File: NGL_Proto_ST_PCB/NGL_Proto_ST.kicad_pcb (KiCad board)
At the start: 2 copper layers, 113 x 70 mm, 138 parts, among them J1 Conn_01x08_Male, J2 Conn_01x04_Male, J3 227161-2, J4 Conn_01x06_Male, J5 Conn_01x04_Male, J6 Conn_01x03_Male, M1 ROB-08449, SW3 SW_Push, SW4 SW_Push, T1 RU1C002UNTCL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

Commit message: Début ajout modifs de la review
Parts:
- removed G2: LOGO, Lib_NGL_EURO:NGL_neg
- added TP10: GND, Connector_PinHeader_2.54mm:PinHeader_1x01_P2.54mm_Vertical, B.Cu at (104.5, 106.0)
- added TP13: GND, Connector_PinHeader_2.54mm:PinHeader_1x01_P2.54mm_Vertical, B.Cu at (103.0, 63.0)
- added TP14: GND, Connector_PinHeader_2.54mm:PinHeader_1x01_P2.54mm_Vertical, B.Cu at (210.0, 64.0)
- added TP9: GND, Connector_PinHeader_2.54mm:PinHeader_1x01_P2.54mm_Vertical, B.Cu at (209.5, 112.5)
- R10P1: value 590 -> NC
- R2: value 442R -> 348R
- R2P1: value 1K -> NC
- TP1: value TestPoint -> IN
- TP11: value TestPoint -> OUT_DIFF
- TP12: value TestPoint -> RECT_DIFF
- TP2: value TestPoint -> IN_ADC
- TP3: value TestPoint -> OUT
- TP4: value TestPoint -> IN_ADC_DIFF
- TP5: value TestPoint -> RECT
- TP6: renamed from TPP3; value TestPointPad -> CLK_GEN
- TP7: value TestPoint -> +3.3V
- TP8: value TestPoint -> -3.3V
- TPP2: value TestPointPad -> +BATT
- TPP4: value TestPointPad -> GND
- moved C16 43.8 mm to (121.2, 92.3), turned to 270 degrees
- moved U6 36.5 mm to (126.4, 91.5)
- moved C17 24.5 mm to (131.8, 94.5), turned to 270 degrees
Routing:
- net -3V3: track 234.2 -> 64.5 mm, vias 6 -> 4
- net +3V3: track 434.9 -> 401.4 mm
- net Net-(C16-Pad2): track 13.4 -> 0.00 mm
- net Net-(C16-Pad1): track 11.3 -> 0.00 mm
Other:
- board text removed: "+3.3V"
- board text removed: "-3.3V"
- board text removed: "DIFF"
- board text removed: "SENS"

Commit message: Commit avand 2° dsn
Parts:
- J2: footprint Connector_PinHeader_2.54mm:PinHeader_1x04_P2.54mm_Vertical -> Connector_PinHeader_2.54mm:PinHeader_1x06_P2.54mm_Vertical
- moved TP9 47.2 mm to (165.8, 94.6)
- moved C7 11.8 mm to (126.5, 57.0), turned to 270 degrees
- moved C4 11.3 mm to (115.0, 60.0), turned to 270 degrees
- moved J2 1.74 mm to (207.5, 108.5)
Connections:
- C19 pad 1: /ESP32/EN -> EN
- J2 pad 2: UART_TX -> BOOT
- J2 pad 3: UART_RX -> UART_TX
- J2 pad 4: +3V3 -> UART_RX
- R17 pad 2: /ESP32/EN -> EN
- SW3 pad 2: /ESP32/EN -> EN
- SW4 pad 1: Net-(SW4-Pad1) -> BOOT
- U4 pad 25: Net-(SW4-Pad1) -> BOOT
- U4 pad 3: /ESP32/EN -> EN
- U4 pad 31: CLOCK_GEN -> Net-(U4-Pad31)
- U4 pad 8: Net-(U4-Pad8) -> CLOCK_GEN
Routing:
- net OUT_NTC: track 131.9 -> 0.00 mm
- net CLOCK_GEN: track 120.4 -> 0.00 mm
- net INH: track 118.2 -> 0.00 mm
- net OUT_BAT: track 107.0 -> 0.00 mm, vias 1 -> 0
- net CLK: track 91.2 -> 0.00 mm, vias 1 -> 0
- net CS_R2: track 90.1 -> 0.00 mm, vias 1 -> 0
- net MOSI: track 82.9 -> 0.00 mm
- net CURRENT_3: track 71.6 -> 0.00 mm, vias 1 -> 0
- net OUT_SENS: track 71.6 -> 0.00 mm, vias 1 -> 0
- net DIFF-: track 63.6 -> 0.00 mm, vias 1 -> 0
- net -3V3: track 64.5 -> 120.6 mm
- net DIFF+: track 53.8 -> 0.00 mm
- net CS_R10: track 53.7 -> 0.00 mm, vias 2 -> 0
- net Net-(JP8-Pad1): track 51.2 -> 0.00 mm, vias 1 -> 0
- net R10_OUT: track 43.6 -> 0.00 mm, vias 1 -> 0
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- removed copper zone on B.Cu, net -BATT
- removed copper zone on F.Cu, net -BATT
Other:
- board text added: "BOOT"
- board text added: "EN"
- board text removed: "MISO"

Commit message: avant 3° DSN
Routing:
- added copper zone on F.Cu, net -BATT
- added copper zone on B.Cu, net Net-(D1-Pad2)
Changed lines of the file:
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@@
     (42 Eco1.User user hide)
     (43 Eco2.User user hide)
-    (44 Edge.Cuts user)
+    (44 Edge.Cuts user hide)
     (45 Margin user hide)
     (46 B.CrtYd user)
@@
     (fp_line (start -1.9939 -2.159) (end -3.0988 -2.159) (layer F.Fab) (width 0.1))
     (fp_line (start -1.9939 -1.651) (end -1.9939 -2.159) (layer F.Fab) (width 0.1))
-    (fp_text user * (at -2.7178 -3.606) (layer F.SilkS)
-      (effects (font (size 1 1) (thickness 0.15)))
-    )
     (fp_text user * (at -5.55 -1.6) (layer F.SilkS)
       (effects (font (size 1 1) (thickness 0.15)))
@@
       (effects (font (size 1 1) (thickness 0.15)))
     )
-    (fp_text user * (at -2.7178 -3.606) (layer F.SilkS)
-      (effects (font (size 1 1) (thickness 0.15)))
-    )
     (fp_text user "Copyright 2021 Accelerated Designs. All rights reserved." (at 0 0) (layer Cmts.User) hide
       (effects (font (size 0.127 0.127) (thickness 0.002)))
@@
       )
     )
+  )
+  (zone (net 11) (net_name -BATT) (layer F.Cu) (hatch edge 0.508)
+    (connect_pads (clearance 0.15))
+    (min_thickness 0.15)
+    (fill yes (arc_segments 32) (thermal_gap 0.2) (thermal_bridge_width 0.2))
+    (polygon
+      (pts
+        (xy 212.5 120) (xy 100 119.5) (xy 99.5 50) (xy 213 50)
+      )
+    )
+  )
+  (zone (net 11) (net_name "Net-(D1-Pad2)") (layer B.Cu) (hatch edge 0.508)
+    (connect_pads (clearance 0.15))
+    (min_thickness 0.15)
+    (fill yes (arc_segments 32) (thermal_gap 0.2) (thermal_bridge_width 0.2))
+    (polygon
+      (pts
+        (xy 212.5 120) (xy 100 119.5) (xy 99.5 50) (xy 213 50)
+      )
+    )

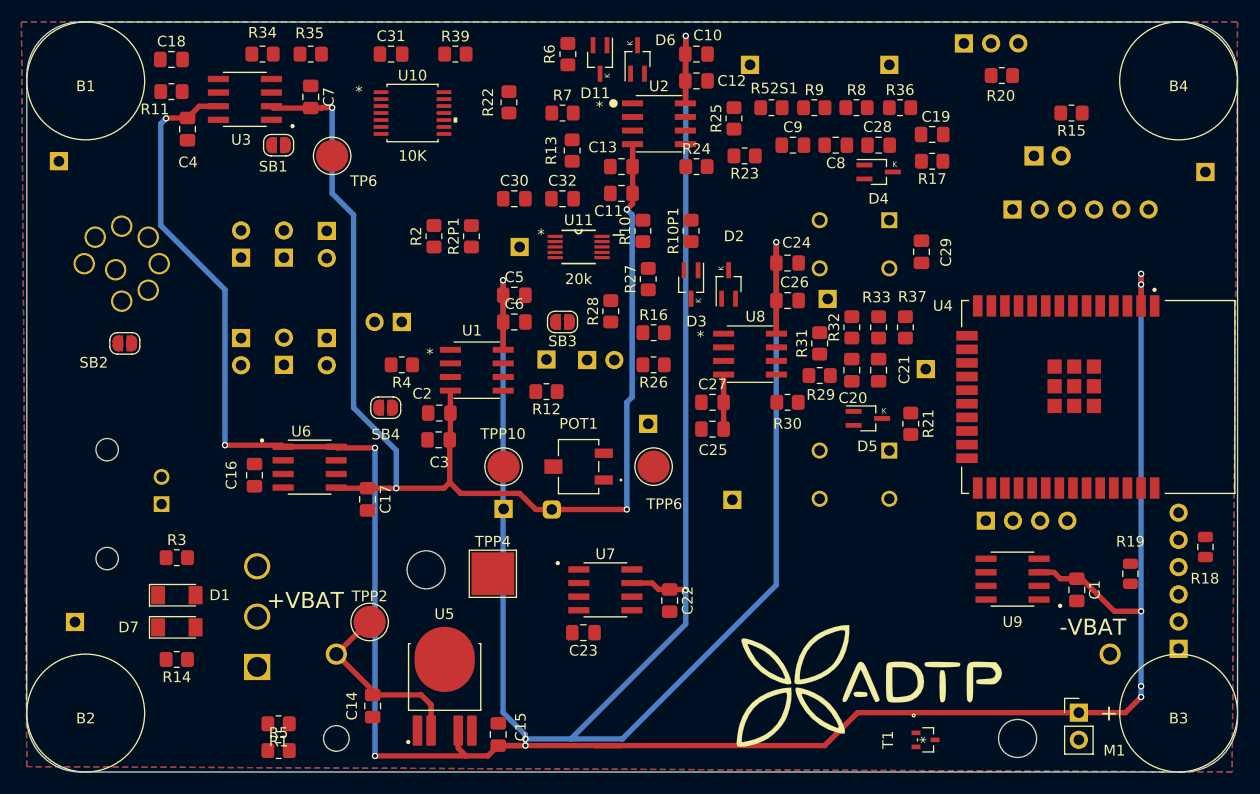
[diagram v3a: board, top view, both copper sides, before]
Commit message: tut router même masse. Attente sully pour commander
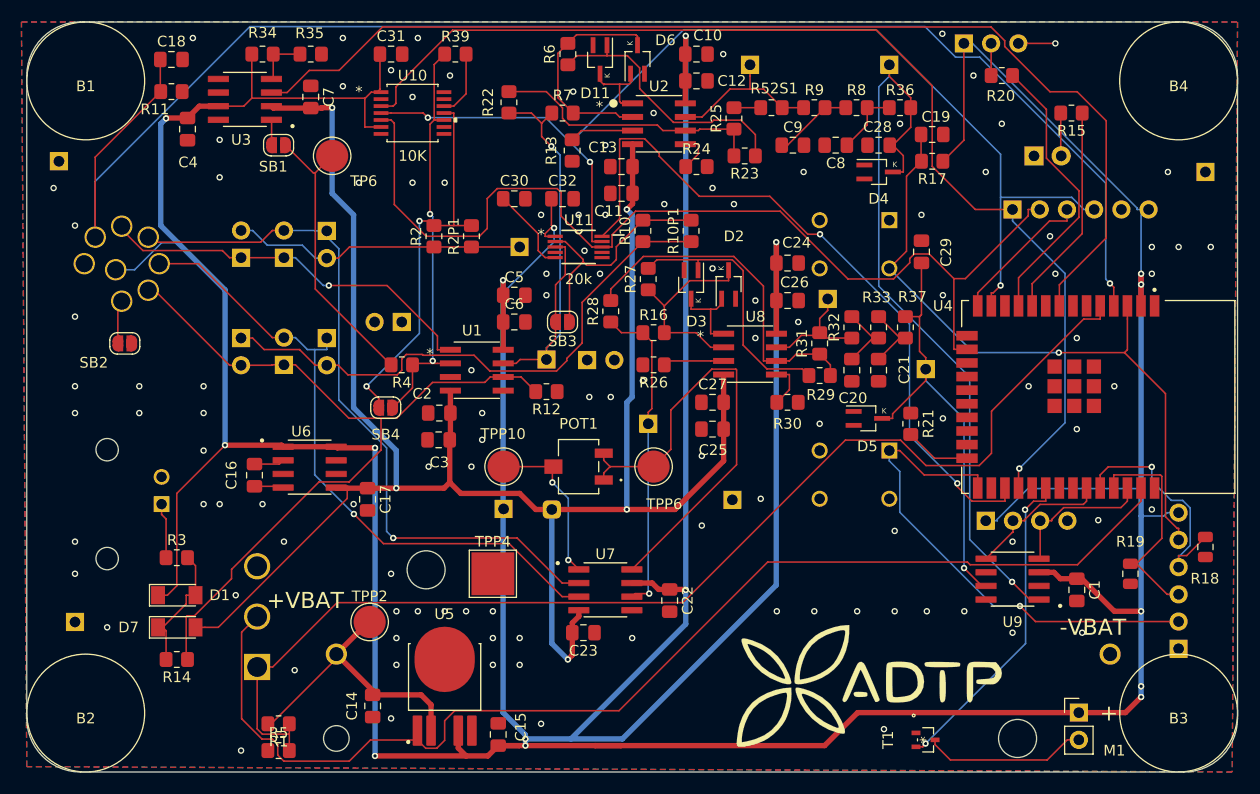
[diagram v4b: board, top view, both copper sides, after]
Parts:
- added G***: LOGO, Lib_NGL_ST:BGM_12345, F.Cu at (68.8, 54.8)
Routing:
- net OUT_NTC: track 0.00 -> 142.5 mm, vias 0 -> 1
- net +3V3: track 418.2 -> 544.0 mm, vias 15 -> 16
- net INH: track 0.00 -> 110.4 mm
- net OUT_BAT: track 0.00 -> 109.1 mm
- net CS_R2: track 0.00 -> 103.9 mm, vias 0 -> 1
- net CLOCK_GEN: track 0.00 -> 103.5 mm
- net CLK: track 0.00 -> 103.0 mm, vias 0 -> 3
- net MOSI: track 0.00 -> 95.1 mm
- net CURRENT_3: track 0.00 -> 75.4 mm
- net OUT_SENS: track 0.00 -> 70.2 mm, vias 0 -> 1
- net DIFF-: track 0.00 -> 67.8 mm, vias 0 -> 1
- net CS_R10: track 0.00 -> 67.4 mm, vias 0 -> 2
- net EN: track 0.00 -> 63.1 mm, vias 0 -> 1
- net DIFF+: track 0.00 -> 61.1 mm, vias 0 -> 1
- net -3V3: track 120.6 -> 174.2 mm, vias 4 -> 5
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- added copper zone on B.Cu, net -BATT
- removed copper zone on B.Cu, net Net-(D1-Pad2)

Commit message: Mise sur le NAS pour Sully
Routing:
- net MOTEUR: track 30.2 -> 33.3 mm
- net UART_RX: track 22.6 -> 22.1 mm

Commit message: GERBER généré: PRODUCTION
EURO
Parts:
- added R18: 4.7K, Resistor_SMD:R_0805_2012Metric_Pad1.20x1.40mm_HandSolder, F.Cu at (126.6, 97.2)
- added R19: 4.7K, Resistor_SMD:R_0805_2012Metric_Pad1.20x1.40mm_HandSolder, F.Cu at (141.3, 62.9)
- added TP15: SDO, Connector_PinHeader_2.54mm:PinHeader_1x01_P2.54mm_Vertical, B.Cu at (144.4, 62.1)
- moved R39 1.17 mm to (141.2, 53.2)
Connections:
- J4 pad 1: CS_R2 -> CS_SPARE
- R39 pad 1: R2_OUT -> R2_IN
- U4 pad 23: Net-(U4-Pad23) -> CS_SPARE
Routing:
- net CS_SPARE: track 0.00 -> 36.0 mm, vias 0 -> 1
- net Net-(R19-Pad2): track 0.00 -> 22.0 mm, vias 0 -> 1
- net +3V3: track 543.7 -> 558.3 mm, vias 16 -> 18
- net R2_IN: track 36.4 -> 45.1 mm
- net R2_OUT: track 38.8 -> 32.3 mm
- net Net-(R18-Pad1): track 0.00 -> 5.59 mm
- net -3V3: track 174.2 -> 176.3 mm
- net CLK: track 102.9 -> 104.0 mm
- net INH: track 110.4 -> 111.3 mm
- net CS_R2: track 103.9 -> 103.3 mm, vias 1 -> 2
- net MISO: track 13.4 -> 12.8 mm
- net Net-(D11-Pad2): track 25.2 -> 25.8 mm
- net Net-(R52S1-Pad2): track 15.1 -> 15.6 mm
- net -BATT: vias 112 -> 120
